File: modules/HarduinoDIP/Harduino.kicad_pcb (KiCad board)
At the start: 2 copper layers, 40.6 x 40.6 mm, 42 parts, among them J1 2, J10 11, J11 12, J12 13, J13 A0, J14 A1, J15 A2, J16 A3, J17 A4, J18 A5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

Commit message: Some changes
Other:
- board text added: "08.03.2020"
- board text removed: "12.10.2019"
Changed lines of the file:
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@@
     (visible_elements 7FFFFFFF)
     (pcbplotparams
-      (layerselection 0x00000_fffffffe)
+      (layerselection 0x010fc_ffffffff)
       (usegerberextensions false)
       (usegerberattributes false)
@@
       (hpglpenspeed 20)
       (hpglpendiameter 15.000000)
-      (psnegative true)
+      (psnegative false)
       (psa4output false)
       (plotreference true)
@@
       (padsonsilk false)
       (subtractmaskfromsilk false)
-      (outputformat 4)
+      (outputformat 1)
       (mirror false)
-      (drillshape 1)
+      (drillshape 0)
       (scaleselection 1)
-      (outputdirectory ""))
+      (outputdirectory "harduinodip/"))
   )
   (net 0 "")
@@
   )
   (gr_poly (pts (xy 110.12 48.7) (xy 110.83 49.72) (xy 111.05 50.04) (xy 111.24 50.22) (xy 111.3 50.26) (xy 111.73 50.39) (xy 111.77 50.37) (xy 111.77 50.28) (xy 111.58 49.85) (xy 111.28 49.2) (xy 112.09 50.19) (xy 112.29 50.41) (xy 112.41 50.51) (xy 112.49 50.54) (xy 112.67 50.55) (xy 112.89 50.61) (xy 112.85 50.49) (xy 112.34 49.6) (xy 113.11 50.44) (xy 113.27 50.63) (xy 113.36 50.71) (xy 113.47 50.76) (xy 113.91 50.81) (xy 114.37 50.83) (xy 114.85 50.23) (xy 115 50.08) (xy 114.99 50.16) (xy 114.85 50.49) (xy 114.77 50.66) (xy 114.76 50.74) (xy 114.84 50.75) (xy 115.24 50.73) (xy 115.59 50.62) (xy 116.26 50.05) (xy 116.14 50.34) (xy 115.71 50.99) (xy 115.38 51.05) (xy 114.77 51.1) (xy 114.58 51.17) (xy 114.8 51.23) (xy 116.13 51.45) (xy 116.45 51.52) (xy 116.58 51.62) (xy 116.6 51.79) (xy 116.58 51.95) (xy 116.52 52.03) (xy 116.47 52.05) (xy 116.43 52.13) (xy 116.43 52.23) (xy 116.37 52.28) (xy 116.18 52.33) (xy 115.56 52.44) (xy 115.27 52.52) (xy 115.14 52.64) (xy 115.11 52.7) (xy 115.08 52.85) (xy 115.09 53.02) (xy 114.76 56.79) (xy 114.81 53.4) (xy 114.8 53.12) (xy 114.79 52.93) (xy 114.78 52.89) (xy 114.74 52.85) (xy 114.69 52.97) (xy 114.66 53.3) (xy 114.63 53.79) (xy 114.6 55.17) (xy 114.58 55.7) (xy 114.54 56.03) (xy 114.51 55.85) (xy 114.48 55.17) (xy 114.48 54.29) (xy 114.46 53.07) (xy 114.3 53.11) (xy 114.19 53.11) (xy 114.12 53.06) (xy 114.05 52.93) (xy 113.81 52.3) (xy 114.12 51.9) (xy 114.08 52.13) (xy 114.07 52.29) (xy 114.07 52.36) (xy 114.14 52.49) (xy 114.29 52.7) (xy 115.2 52.31) (xy 115.33 52.24) (xy 115.38 52.18) (xy 115.27 52.14) (xy 115.48 52.1) (xy 116 52.09) (xy 116.12 52.07) (xy 116.21 52.02) (xy 116.24 51.96) (xy 116.21 51.84) (xy 116.05 51.74) (xy 115.78 51.63) (xy 115.38 51.55) (xy 115.14 51.54) (xy 115 51.56) (xy 114.95 51.6) (xy 114.88 51.7) (xy 114.83 51.71) (xy 114.77 51.71) (xy 114.65 51.66) (xy 114.5 51.56) (xy 114.46 51.5) (xy 114.45 51.46) (xy 114.39 51.43) (xy 114.31 51.4) (xy 113.82 51.38) (xy 113.37 51.39) (xy 113.23 51.41) (xy 113.11 51.44) (xy 113.13 51.48) (xy 113.34 51.52) (xy 113.64 51.54) (xy 114.15 51.55) (xy 113.73 51.7) (xy 113.73 51.73) (xy 113.93 51.75) (xy 113.94 51.78) (xy 113.7 51.9) (xy 113.64 51.97) (xy 113.51 52.16) (xy 113.31 52.59) (xy 112.88 53.64) (xy 112.66 54.29) (xy 112.61 54.46) (xy 112.58 54.6) (xy 112.63 54.68) (xy 112.68 54.65) (xy 112.72 54.58) (xy 112.81 54.36) (xy 112.99 53.85) (xy 113.3 53.02) (xy 113.26 53.28) (xy 113.01 54.28) (xy 112.95 54.49) (xy 112.89 54.83) (xy 112.87 54.95) (xy 112.87 55.06) (xy 112.92 55.12) (xy 112.98 55.04) (xy 113.02 54.89) (xy 113.12 54.52) (xy 113.28 53.8) (xy 113.31 53.8) (xy 113.16 54.96) (xy 113.09 55.41) (xy 113.48 55.98) (xy 113.64 56.28) (xy 113.03 55.57) (xy 112.33 54.68) (xy 110.69 54.75) (xy 112.09 54.45) (xy 112.3 54.38) (xy 112.38 54.16) (xy 112.67 53.28) (xy 112.92 52.43) (xy 113.08 51.76) (xy 112.35 51.19) (xy 112.71 51.15) (xy 113.16 51.17) (xy 113.64 51.18) (xy 111.72 50.76) (xy 110.92 50.57) (xy 110.49 49.6)) (layer F.SilkS) (width 0.1))
-  (gr_text 12.10.2019 (at 115.57 66.04 90) (layer F.Cu)
+  (gr_text 08.03.2020 (at 115.57 66.04 90) (layer F.Cu)
     (effects (font (size 1.5 1.5) (thickness 0.3)))
   )

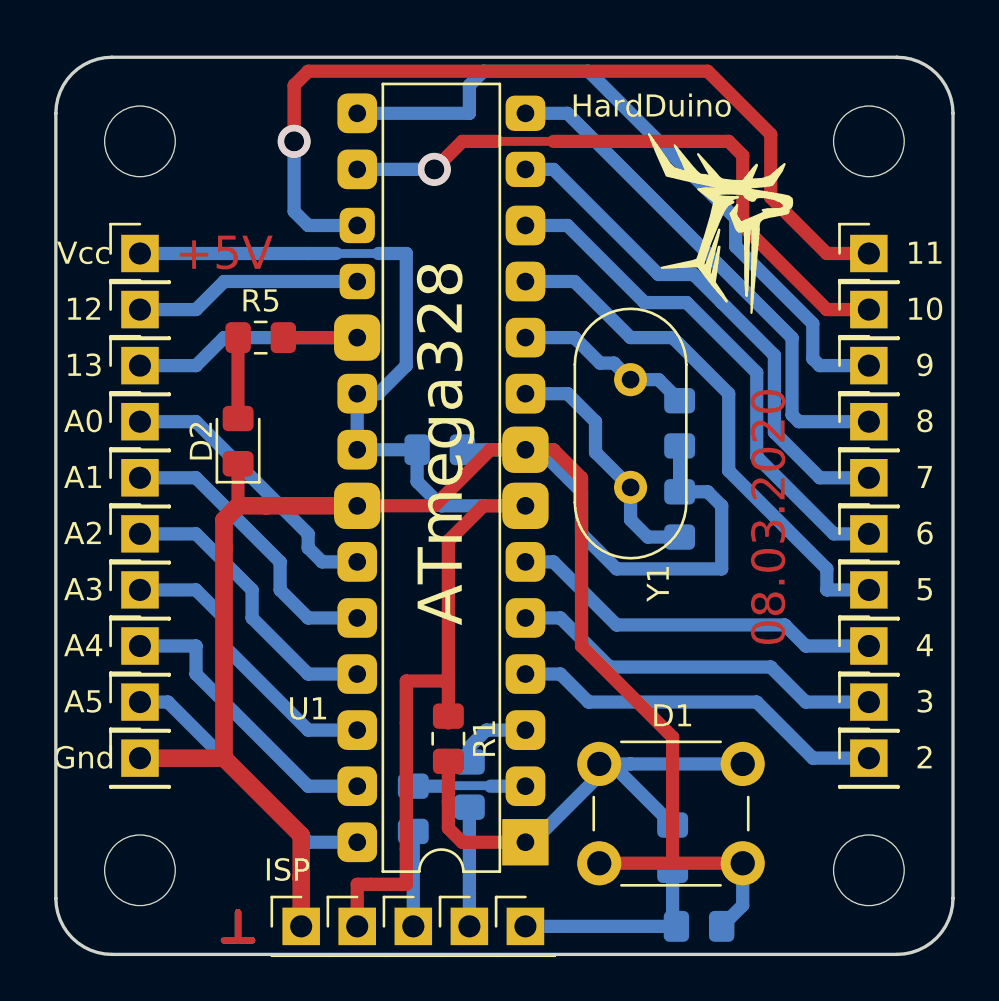
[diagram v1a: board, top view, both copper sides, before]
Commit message: Fix some tracks
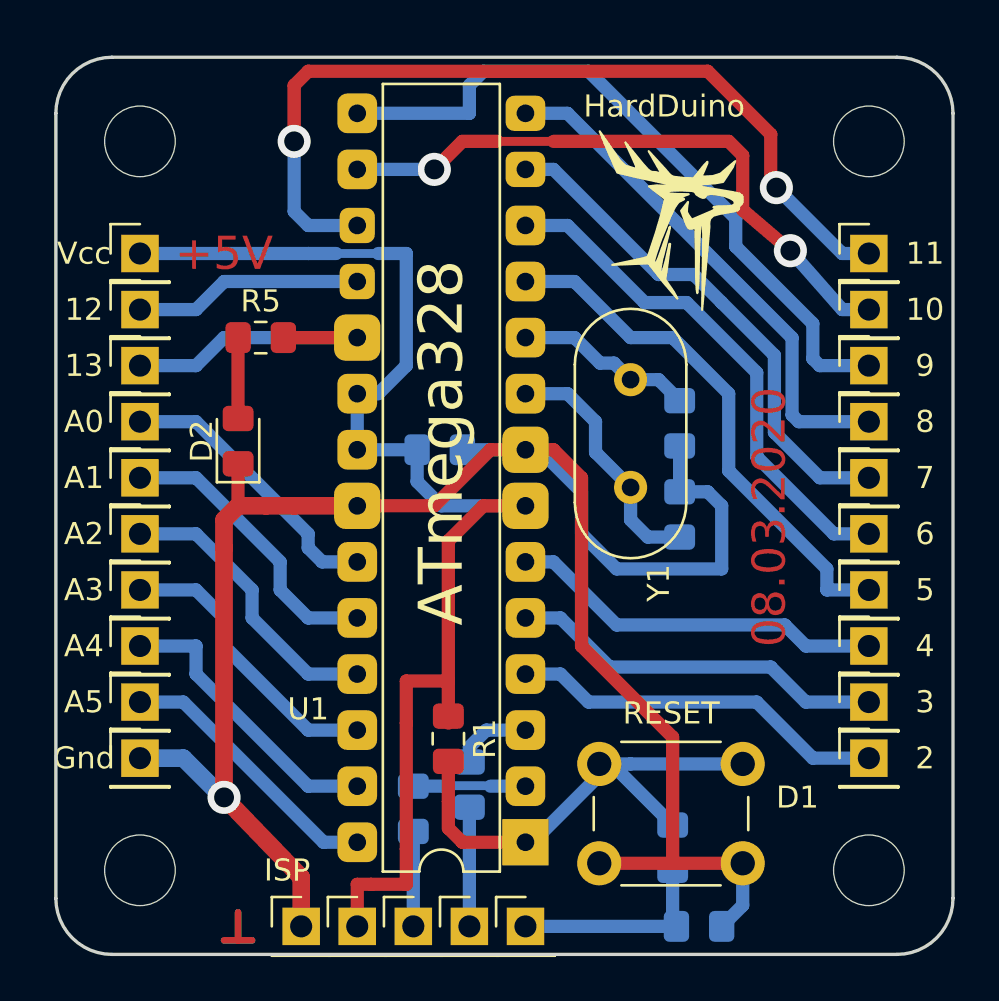
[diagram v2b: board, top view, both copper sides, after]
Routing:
- net GND: track 94.7 -> 95.4 mm, vias 0 -> 1
- net Net-(J10-Pad1): track 40.2 -> 39.8 mm, vias 1 -> 2
- net Net-(J9-Pad1): track 28.7 -> 28.3 mm, vias 1 -> 2
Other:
- board text added: "RESET"

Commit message: HardDuino polishing
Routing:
- net Net-(J9-Pad1): track 28.3 -> 26.8 mm
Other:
- board text added: "07.05.2020"
- board text added: "d7dd6d"
- board text added: "v2"
- board text removed: "08.03.2020"
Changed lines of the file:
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@@
-(kicad_pcb (version 20171130) (host pcbnew "(5.1.4)-1")
+(kicad_pcb (version 20171130) (host pcbnew "(5.1.5)-3")
   (general
     (thickness 1.6)
-    (drawings 40)
-    (tracks 210)
+    (drawings 42)
+    (tracks 212)
     (zones 0)
     (modules 42)
@@
     (via_min_size 0.4)
     (via_min_drill 0.3)
-    (user_via 1.5 0.9)
+    (user_via 1.6 0.9)
+    (user_via 2 0.9)
     (uvia_size 0.3)
     (uvia_drill 0.1)
@@
     (visible_elements 7FFFFFFF)
     (pcbplotparams
-      (layerselection 0x010fc_ffffffff)
+      (layerselection 0x00000_7fffffff)
       (usegerberextensions false)
       (usegerberattributes false)
@@
       (hpglpenspeed 20)
       (hpglpendiameter 15.000000)
-      (psnegative false)
+      (psnegative true)
       (psa4output false)
       (plotreference true)
@@
       (padsonsilk false)
       (subtractmaskfromsilk false)
-      (outputformat 1)
-      (mirror false)
-      (drillshape 0)
+      (outputformat 4)
+      (mirror true)
+      (drillshape 1)
       (scaleselection 1)
-      (outputdirectory "harduinodip/"))
+      (outputdirectory "pdf/"))
   )
   (net 0 "")
@@
     )
   )
+  (gr_text v2 (at 115.57 64.77 90) (layer F.Cu)
+    (effects (font (size 1.5 1.5) (thickness 0.3)))
+  )
+  (gr_text d7dd6d (at 116.84 59.69 90) (layer F.Cu)
+    (effects (font (size 1 1) (thickness 0.2)))
+  )
   (gr_text RESET (at 111.125 74.93) (layer F.SilkS)
     (effects (font (size 1 1) (thickness 0.15)))
   )
   (gr_poly (pts (xy 107.885 48.5675) (xy 108.595 49.5875) (xy 108.815 49.9075) (xy 109.005 50.0875) (xy 109.065 50.1275) (xy 109.495 50.2575) (xy 109.535 50.2375) (xy 109.535 50.1475) (xy 109.345 49.7175) (xy 109.045 49.0675) (xy 109.855 50.0575) (xy 110.055 50.2775) (xy 110.175 50.3775) (xy 110.255 50.4075) (xy 110.435 50.4175) (xy 110.655 50.4775) (xy 110.615 50.3575) (xy 110.105 49.4675) (xy 110.875 50.3075) (xy 111.035 50.4975) (xy 111.125 50.5775) (xy 111.235 50.6275) (xy 111.675 50.6775) (xy 112.135 50.6975) (xy 112.615 50.0975) (xy 112.765 49.9475) (xy 112.755 50.0275) (xy 112.615 50.3575) (xy 112.535 50.5275) (xy 112.525 50.6075) (xy 112.605 50.6175) (xy 113.005 50.5975) (xy 113.355 50.4875) (xy 114.025 49.9175) (xy 113.905 50.2075) (xy 113.475 50.8575) (xy 113.145 50.9175) (xy 112.535 50.9675) (xy 112.345 51.0375) (xy 112.565 51.0975) (xy 113.895 51.3175) (xy 114.215 51.3875) (xy 114.345 51.4875) (xy 114.365 51.6575) (xy 114.345 51.8175) (xy 114.285 51.8975) (xy 114.235 51.9175) (xy 114.195 51.9975) (xy 114.195 52.0975) (xy 114.135 52.1475) (xy 113.945 52.1975) (xy 113.325 52.3075) (xy 113.035 52.3875) (xy 112.905 52.5075) (xy 112.875 52.5675) (xy 112.845 52.7175) (xy 112.855 52.8875) (xy 112.525 56.6575) (xy 112.575 53.2675) (xy 112.565 52.9875) (xy 112.555 52.7975) (xy 112.545 52.7575) (xy 112.505 52.7175) (xy 112.455 52.8375) (xy 112.425 53.1675) (xy 112.395 53.6575) (xy 112.365 55.0375) (xy 112.345 55.5675) (xy 112.305 55.8975) (xy 112.275 55.7175) (xy 112.245 55.0375) (xy 112.245 54.1575) (xy 112.225 52.9375) (xy 112.065 52.9775) (xy 111.955 52.9775) (xy 111.885 52.9275) (xy 111.815 52.7975) (xy 111.575 52.1675) (xy 111.885 51.7675) (xy 111.845 51.9975) (xy 111.835 52.1575) (xy 111.835 52.2275) (xy 111.905 52.3575) (xy 112.055 52.5675) (xy 112.965 52.1775) (xy 113.095 52.1075) (xy 113.145 52.0475) (xy 113.035 52.0075) (xy 113.245 51.9675) (xy 113.765 51.9575) (xy 113.885 51.9375) (xy 113.975 51.8875) (xy 114.005 51.8275) (xy 113.975 51.7075) (xy 113.815 51.6075) (xy 113.545 51.4975) (xy 113.145 51.4175) (xy 112.905 51.4075) (xy 112.765 51.4275) (xy 112.715 51.4675) (xy 112.645 51.5675) (xy 112.595 51.5775) (xy 112.535 51.5775) (xy 112.415 51.5275) (xy 112.265 51.4275) (xy 112.225 51.3675) (xy 112.215 51.3275) (xy 112.155 51.2975) (xy 112.075 51.2675) (xy 111.585 51.2475) (xy 111.135 51.2575) (xy 110.995 51.2775) (xy 110.875 51.3075) (xy 110.895 51.3475) (xy 111.105 51.3875) (xy 111.405 51.4075) (xy 111.915 51.4175) (xy 111.495 51.5675) (xy 111.495 51.5975) (xy 111.695 51.6175) (xy 111.705 51.6475) (xy 111.465 51.7675) (xy 111.405 51.8375) (xy 111.275 52.0275) (xy 111.075 52.4575) (xy 110.645 53.5075) (xy 110.425 54.1575) (xy 110.375 54.3275) (xy 110.345 54.4675) (xy 110.395 54.5475) (xy 110.445 54.5175) (xy 110.485 54.4475) (xy 110.575 54.2275) (xy 110.755 53.7175) (xy 111.065 52.8875) (xy 111.025 53.1475) (xy 110.775 54.1475) (xy 110.715 54.3575) (xy 110.655 54.6975) (xy 110.635 54.8175) (xy 110.635 54.9275) (xy 110.685 54.9875) (xy 110.745 54.9075) (xy 110.785 54.7575) (xy 110.885 54.3875) (xy 111.045 53.6675) (xy 111.075 53.6675) (xy 110.925 54.8275) (xy 110.855 55.2775) (xy 111.245 55.8475) (xy 111.405 56.1475) (xy 110.795 55.4375) (xy 110.095 54.5475) (xy 108.455 54.6175) (xy 109.855 54.3175) (xy 110.065 54.2475) (xy 110.145 54.0275) (xy 110.435 53.1475) (xy 110.685 52.2975) (xy 110.845 51.6275) (xy 110.115 51.0575) (xy 110.475 51.0175) (xy 110.925 51.0375) (xy 111.405 51.0475) (xy 109.485 50.6275) (xy 108.685 50.4375) (xy 108.255 49.4675)) (layer F.SilkS) (width 0.1))
-  (gr_text 08.03.2020 (at 115.57 66.04 90) (layer F.Cu)
-    (effects (font (size 1.5 1.5) (thickness 0.3)))
+  (gr_text 07.05.2020 (at 116.84 72.39 90) (layer F.Cu)
+    (effects (font (size 1 1) (thickness 0.2)))
   )
   (gr_text +5V (at 90.8685 54.102) (layer F.Cu)
@@
   (segment (start 114.046 52.5145) (end 107.3785 45.847) (width 0.6) (layer B.Cu) (net 8))
   (segment (start 101.981 47.752) (end 101.981 46.482) (width 0.6) (layer B.Cu) (net 8))
-  (via (at 100.3935 50.292) (size 1.5) (drill 0.9) (layers F.Cu B.Cu) (net 9))
+  (via (at 100.3935 50.292) (size 2) (drill 0.9) (layers F.Cu B.Cu) (net 9))
   (segment (start 103.251 49.022) (end 105.791 49.022) (width 0.4) (layer F.Cu) (net 9))
   (segment (start 96.901 50.292) (end 100.3935 50.292) (width 0.6) (layer B.Cu) (net 9))
   (segment (start 101.6635 49.022) (end 103.251 49.022) (width 0.6) (layer F.Cu) (net 9))
   (segment (start 100.3935 50.292) (end 101.6635 49.022) (width 0.6) (layer F.Cu) (net 9))
-  (segment (start 114.3635 52.1335) (end 116.5225 53.975) (width 0.6) (layer F.Cu) (net 9))
-  (segment (start 114.3635 49.657) (end 114.3635 52.1335) (width 0.6) (layer F.Cu) (net 9))
-  (segment (start 113.7285 49.022) (end 114.3635 49.657) (width 0.6) (layer F.Cu) (net 9))
-  (segment (start 105.791 49.022) (end 113.7285 49.022) (width 0.6) (layer F.Cu) (net 9))
-  (via (at 116.5225 53.975) (size 1.5) (drill 0.9) (layers F.Cu B.Cu) (net 9))
+  (via (at 116.5225 53.6575) (size 2) (drill 0.9) (layers F.Cu B.Cu) (net 9))
   (segment (start 118.872 56.642) (end 116.5225 53.975) (width 0.6) (layer B.Cu) (net 9))
   (segment (start 120.0785 56.642) (end 118.872 56.642) (width 0.6) (layer B.Cu) (net 9))
+  (segment (start 105.791 49.022) (end 111.252 49.022) (width 0.6) (layer F.Cu) (net 9))
+  (segment (start 115.8875 53.6575) (end 116.5225 53.6575) (width 0.6) (layer F.Cu) (net 9))
+  (segment (start 111.252 49.022) (end 115.8875 53.6575) (width 0.6) (layer F.Cu) (net 9))
   (segment (start 96.901 52.832) (end 94.6785 52.832) (width 0.6) (layer B.Cu) (net 10))
-  (via (at 94.0435 49.022) (size 1.5) (drill 0.9) (layers F.Cu B.Cu) (net 10))
+  (via (at 94.0435 49.022) (size 2) (drill 0.9) (layers F.Cu B.Cu) (net 10))
   (segment (start 94.0435 52.197) (end 94.6785 52.832) (width 0.6) (layer B.Cu) (net 10))
   (segment (start 94.0435 49.022) (end 94.0435 52.197) (width 0.6) (layer B.Cu) (net 10))
@@
   (segment (start 94.0435 46.482) (end 94.6785 45.847) (width 0.6) (layer F.Cu) (net 10))
   (segment (start 94.6785 45.847) (end 112.776 45.847) (width 0.6) (layer F.Cu) (net 10))
-  (segment (start 112.776 45.847) (end 115.6335 48.7045) (width 0.6) (layer F.Cu) (net 10))
-  (segment (start 115.6335 48.7045) (end 115.6335 50.8635) (width 0.6) (layer F.Cu) (net 10))
-  (segment (start 115.6335 50.8635) (end 115.8875 51.1175) (width 0.6) (layer F.Cu) (net 10))
-  (via (at 115.8875 51.1175) (size 1.5) (drill 0.9) (layers F.Cu B.Cu) (net 10))
+  (via (at 115.2525 50.165) (size 2) (drill 0.9) (layers F.Cu B.Cu) (net 10))
   (segment (start 120.0785 54.102) (end 118.872 54.102) (width 0.6) (layer B.Cu) (net 10))
-  (segment (start 118.872 54.102) (end 115.8875 51.1175) (width 0.6) (layer B.Cu) (net 10))
+  (segment (start 115.2525 48.3235) (end 115.2525 50.165) (width 0.6) (layer F.Cu) (net 10))
+  (segment (start 115.22075 48.29175) (end 115.2525 48.3235) (width 0.6) (layer F.Cu) (net 10))
+  (segment (start 112.776 45.847) (end 115.22075 48.29175) (width 0.6) (layer F.Cu) (net 10))
+  (segment (start 116.252499 51.164999) (end 116.569999 51.164999) (width 0.6) (layer B.Cu) (net 10))
+  (segment (start 115.2525 50.165) (end 116.252499 51.164999) (width 0.6) (layer B.Cu) (net 10))
+  (segment (start 116.569999 51.164999) (end 118.745 53.34) (width 0.6) (layer B.Cu) (net 10))
+  (segment (start 118.745 53.34) (end 118.745 53.975) (width 0.6) (layer B.Cu) (net 10))
   (segment (start 87.0585 56.642) (end 89.5985 56.642) (width 0.6) (layer B.Cu) (net 11))
   (segment (start 89.5985 56.642) (end 90.8685 55.372) (width 0.6) (layer B.Cu) (net 11))
@@
   (segment (start 107.061 64.262) (end 107.061 71.882) (width 0.6) (layer F.Cu) (net 21))
   (segment (start 107.061 71.882) (end 111.1885 76.0095) (width 0.6) (layer F.Cu) (net 21))
-  (via (at 90.8685 78.74) (size 1.5) (drill 0.9) (layers F.Cu B.Cu) (net 21))
+  (via (at 90.8685 78.74) (size 2) (drill 0.9) (layers F.Cu B.Cu) (net 21))
   (segment (start 89.027 76.962) (end 90.805 78.74) (width 0.8) (layer B.Cu) (net 21))
   (segment (start 87.0585 76.962) (end 89.027 76.962) (width 0.8) (layer B.Cu) (net 21))
